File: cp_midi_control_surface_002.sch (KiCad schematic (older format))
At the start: 37 parts, among them P1 Power, P2 Analogue, P3 Digital, P4 Communication, P5 PWM, P6 PWM

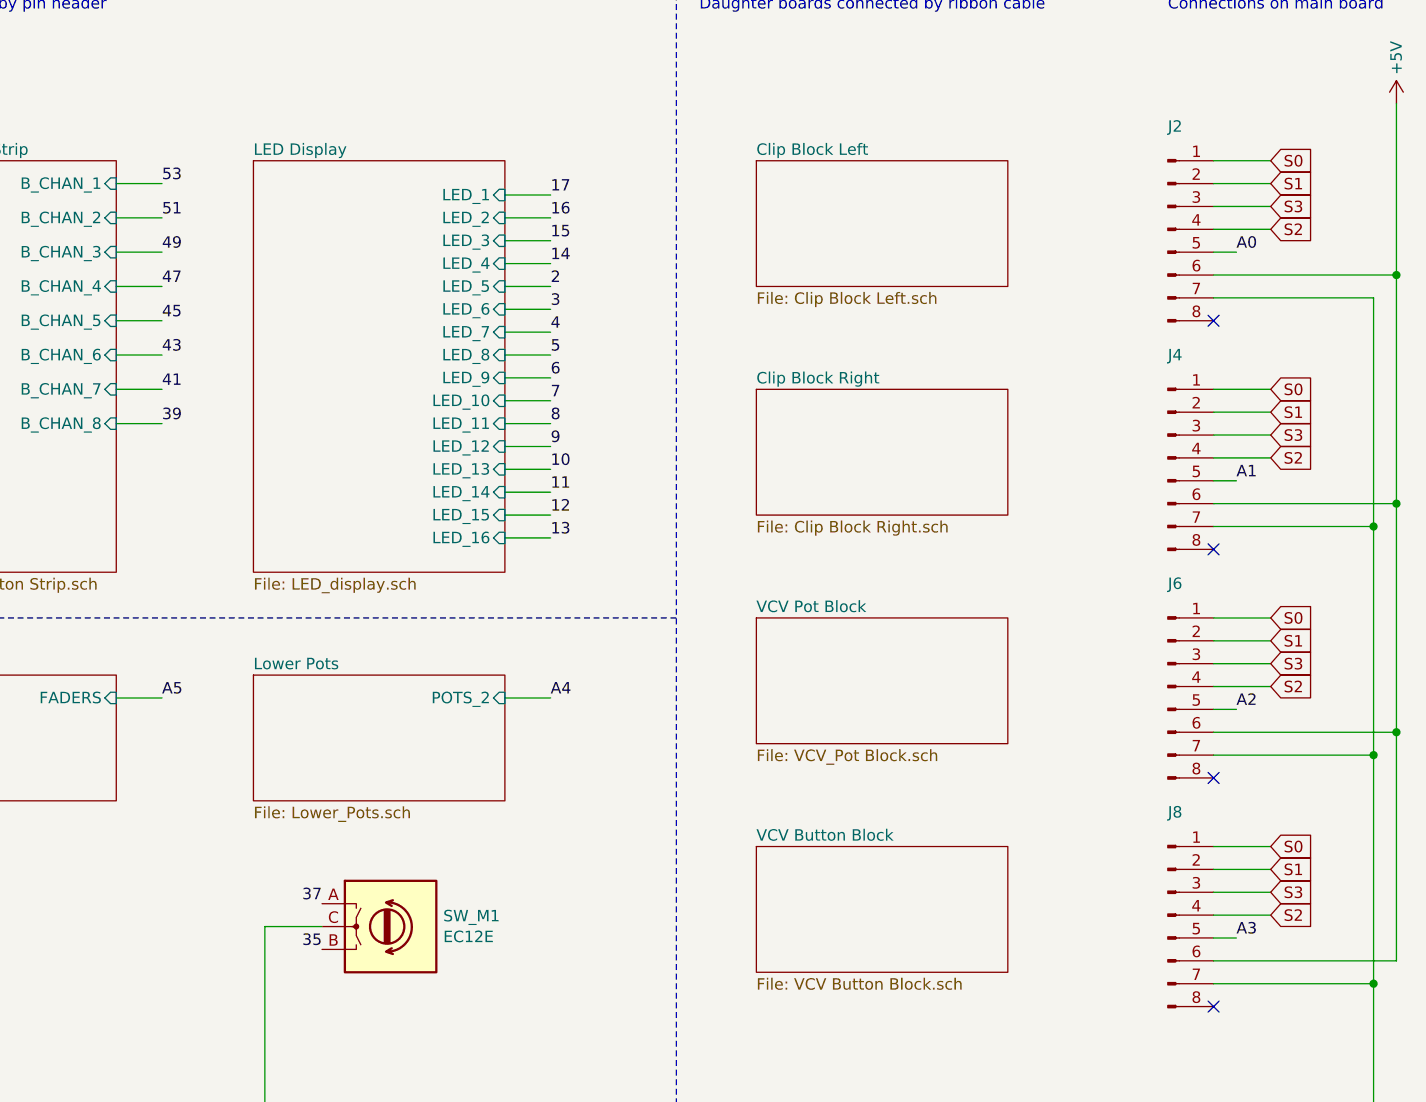
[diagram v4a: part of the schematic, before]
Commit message: Further traces added and reassigned duaghter board connection
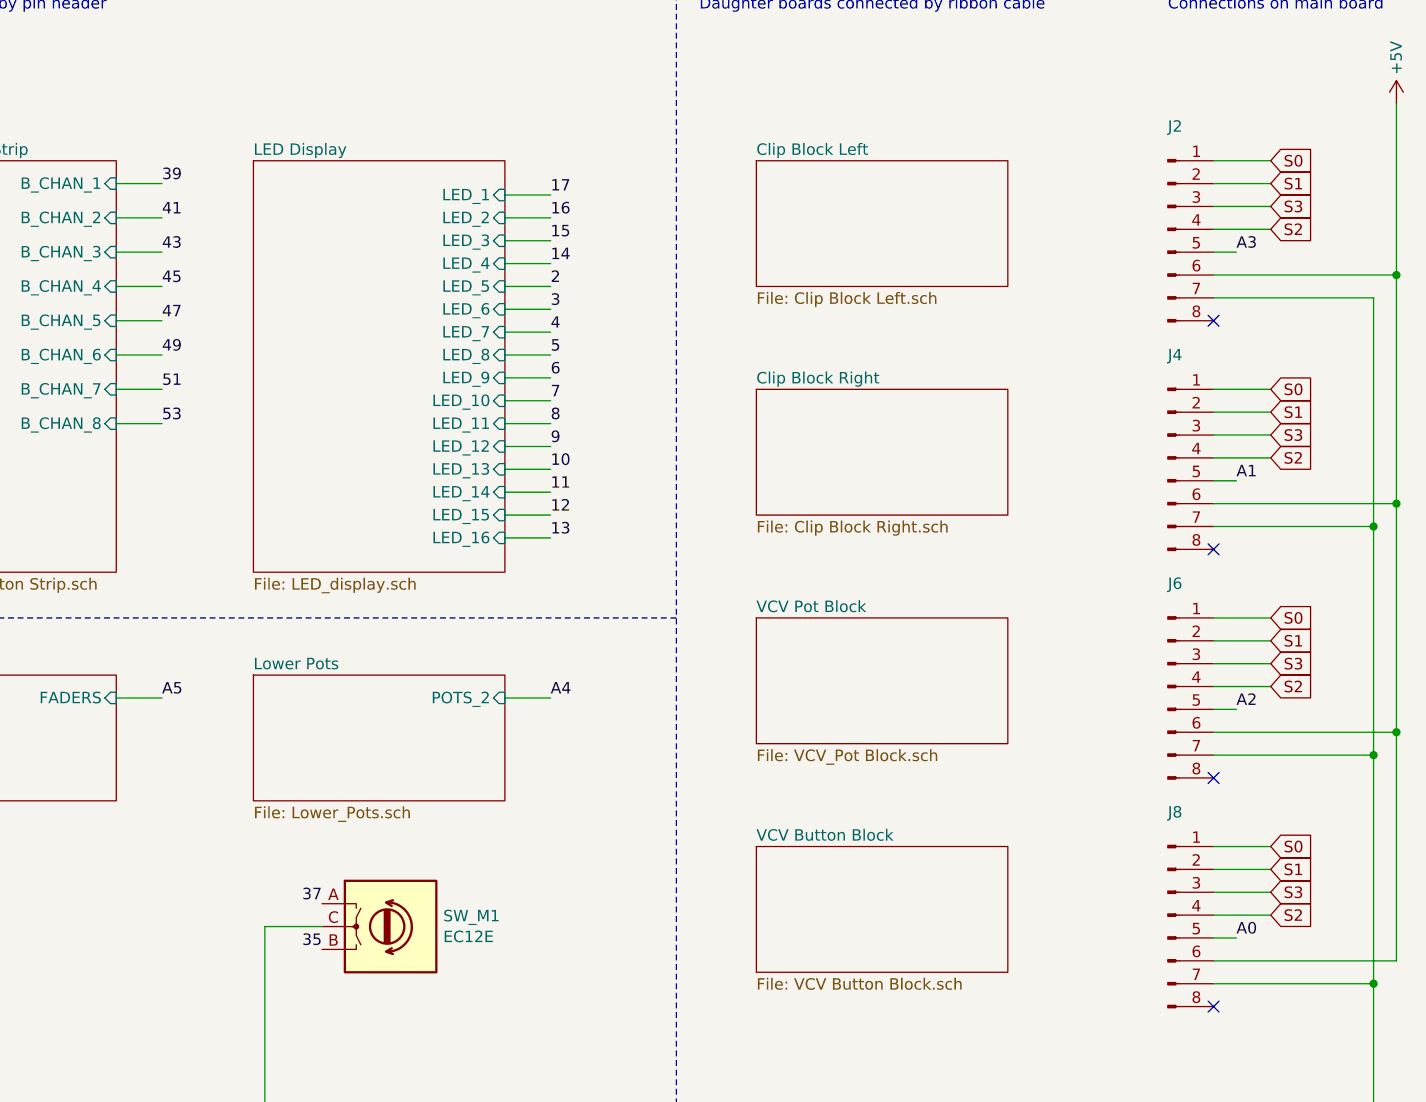
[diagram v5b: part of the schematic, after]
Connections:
- net A0: now also J8.5 (Pin_5); no longer J2.5 (Pin_5)
- net A3: now also J2.5 (Pin_5); no longer J8.5 (Pin_5)
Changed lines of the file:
@@
 Wire Wire Line
 	2250 2400 2050 2400
+Text Label 2250 2400 0    50   ~ 0
+53
+Text Label 2250 2250 0    50   ~ 0
+51
+Text Label 2250 1950 0    50   ~ 0
+47
+Text Label 2250 2100 0    50   ~ 0
+49
+Text Label 2250 1800 0    50   ~ 0
+45
+Text Label 2250 1650 0    50   ~ 0
+43
+Text Label 2250 1500 0    50   ~ 0
+41
 Text Label 2250 1350 0    50   ~ 0
-53
-Text Label 2250 1500 0    50   ~ 0
-51
-Text Label 2250 1800 0    50   ~ 0
-47
-Text Label 2250 1650 0    50   ~ 0
-49
-Text Label 2250 1950 0    50   ~ 0
-45
-Text Label 2250 2100 0    50   ~ 0
-43
-Text Label 2250 2250 0    50   ~ 0
-41
-Text Label 2250 2400 0    50   ~ 0
 39
 NoConn ~ 10450 3750
@@
 Wire Wire Line
 	8650 5050 8650 5750
-Text Label 6950 1650 0    50   ~ 0
+Text Label 6950 4650 0    50   ~ 0
 A0
 $Comp
@@
 	7550 2850 6850 2850
 NoConn ~ 6850 2950
-Text Label 6950 4650 0    50   ~ 0
+Text Label 6950 1650 0    50   ~ 0
 A3
 $Comp

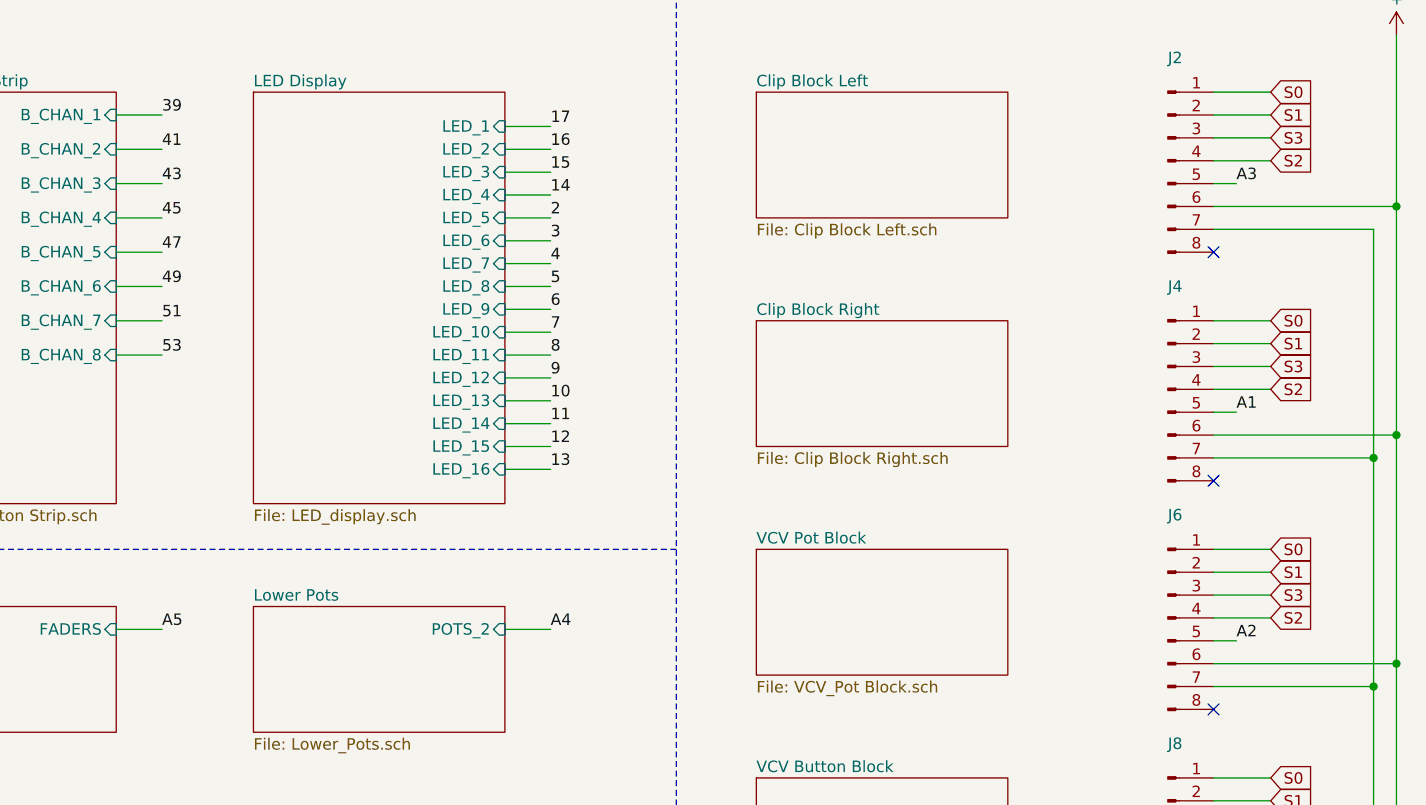
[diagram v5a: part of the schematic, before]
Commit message: Connections complete
All traces mapped and DRC passed apart from interboard errors - should look into fixing those.
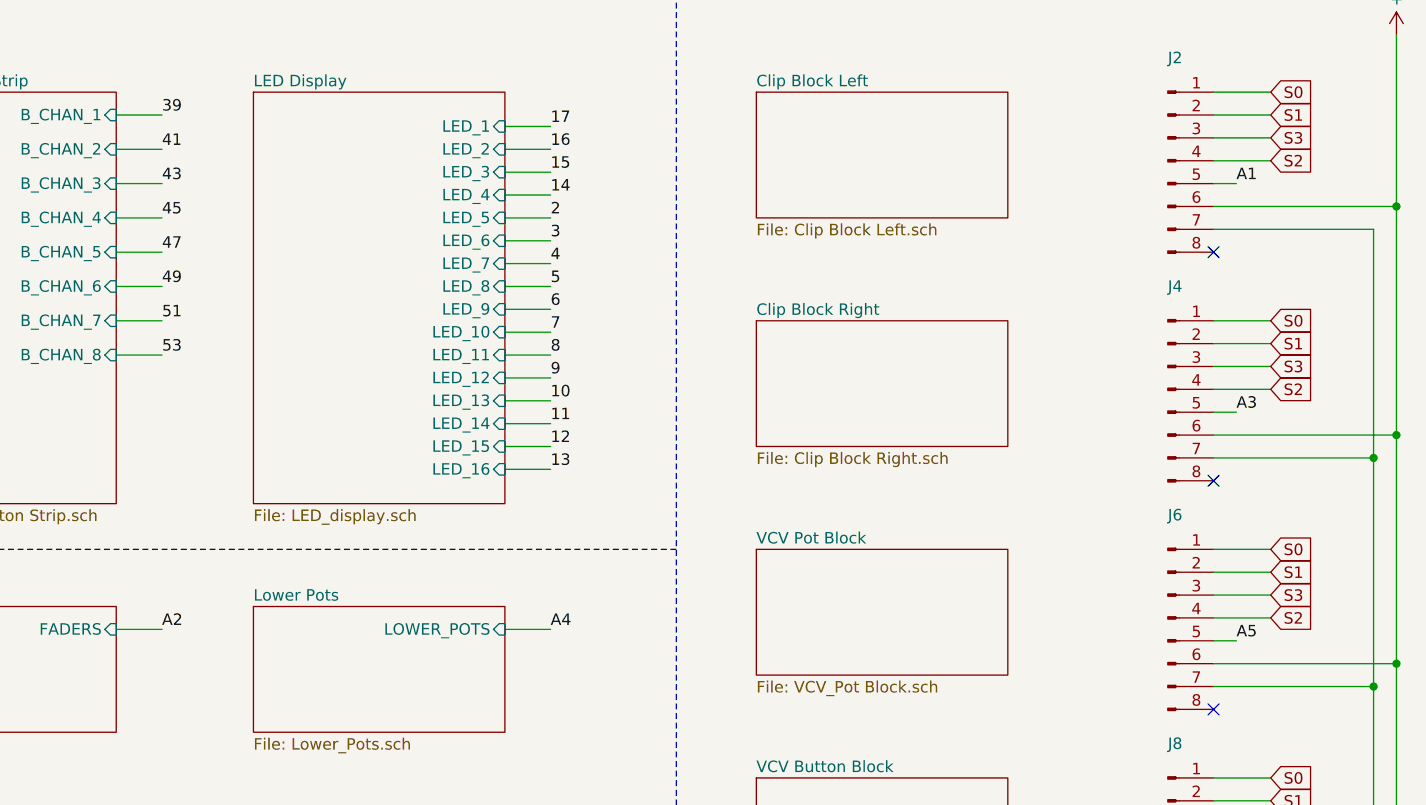
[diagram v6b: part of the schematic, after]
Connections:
- net A1: now also J2.5 (Pin_5); no longer J4.5 (Pin_5)
- net A2: no longer J6.5 (Pin_5)
- net A3: now also J4.5 (Pin_5); no longer J2.5 (Pin_5)
- net A5: now also J6.5 (Pin_5)
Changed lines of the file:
@@
 F0 "Lower Pots" 50
 F1 "Lower_Pots.sch" 0
-F2 "POTS_2" I R 3750 3600 50
+F2 "LOWER_POTS" I R 3750 3600 50
 $EndSheet
 $Sheet
@@
 NoConn ~ 6850 1950
 Text Label 6950 3650 0    50   ~ 0
-A2
+A5
 $Comp
 L Connector:Conn_01x08_Male J6
@@
 NoConn ~ 6850 3950
 Text Label 6950 2650 0    50   ~ 0
-A1
+A3
 $Comp
 L Connector:Conn_01x08_Male J4
@@
 NoConn ~ 6850 2950
 Text Label 6950 1650 0    50   ~ 0
-A3
+A1
 $Comp
 L Connector:Conn_01x08_Male J8
@@
 	10500 4850 10500 5050
 Text Label 2250 3600 0    50   ~ 0
-A5
+A2
 Wire Wire Line
 	2050 3600 2250 3600

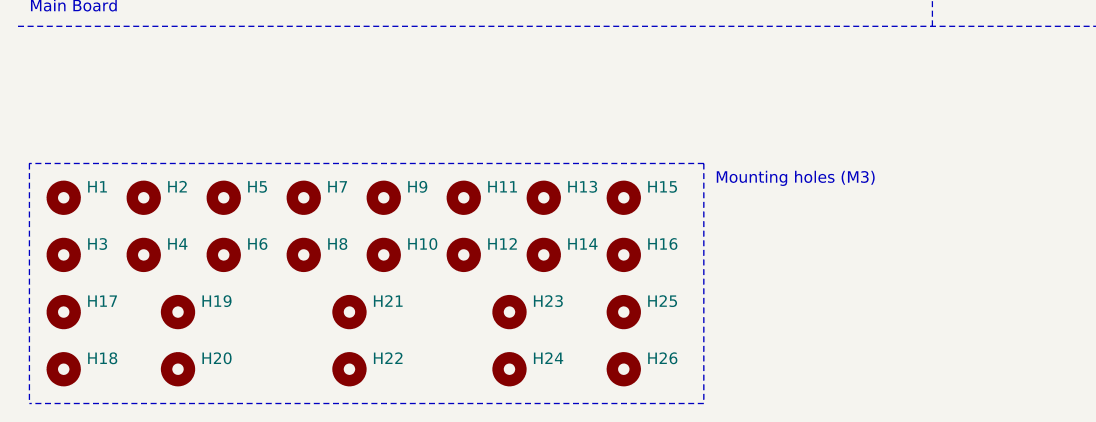
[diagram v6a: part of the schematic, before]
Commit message: Resize boards and update connector
Resized the boards to fit the new modular height and started changing the interboard connectors
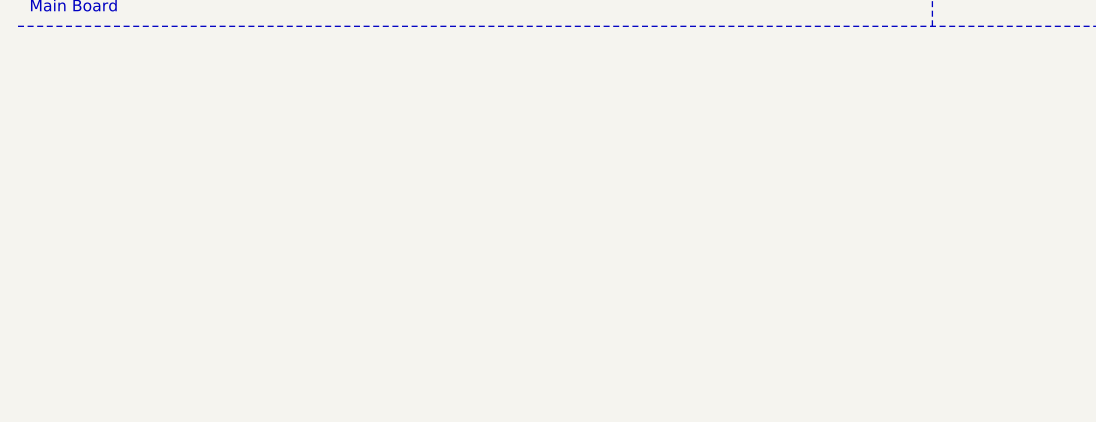
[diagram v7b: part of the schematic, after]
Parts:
- removed H1, H10, H11, H12, H13, H14, H15, H16, H17, H18, H19, H2, H20, H21, H22, H23, H24, H25, H26, H3, H4, H5, H6, H7, H8, H9: ~, cunabulapress-footprints:Mounting_Hole_M3_with_Target, symbol Mechanical:MountingHole
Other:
- note removed: "Mounting holes (M3)"

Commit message: Further cleanup and placement
Removed all the connectors to the rails as they're irrelevant to the top boards.

Added all the support headers.

Need to work out the correct routing for the headers but the placement is correct.
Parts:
- added JX13, JX14, JX15, JX16, JX17, JX18, JX19, JX20, JX21, JX22, JX23, JX24: Conn_02x03_Odd_Even, Connector_PinHeader_2.54mm:PinHeader_2x03_P2.54mm_Vertical, symbol Connector_Generic:Conn_02x03_Odd_Even
- JA2: renamed from J2; footprint cunabulapress-footprints:Connector_TE_Connectivity_Micro-MaTch_8_Position_Female -> Connector_PinHeader_2.54mm:PinHeader_2x03_P2.54mm_Vertical; symbol Connector:Conn_01x08_Male -> Connector:Conn_01x06_Male
- JA4: renamed from J4; footprint cunabulapress-footprints:Connector_TE_Connectivity_Micro-MaTch_8_Position_Female -> Connector_PinHeader_2.54mm:PinHeader_2x03_P2.54mm_Vertical; symbol Connector:Conn_01x08_Male -> Connector:Conn_01x06_Male
- JA6: renamed from J6; footprint cunabulapress-footprints:Connector_TE_Connectivity_Micro-MaTch_8_Position_Female -> Connector_PinHeader_2.54mm:PinHeader_2x03_P2.54mm_Vertical; symbol Connector:Conn_01x08_Male -> Connector:Conn_01x06_Male
- JA8: renamed from J8; footprint cunabulapress-footprints:Connector_TE_Connectivity_Micro-MaTch_8_Position_Female -> Connector_PinHeader_2.54mm:PinHeader_2x03_P2.54mm_Vertical; symbol Connector:Conn_01x08_Male -> Connector:Conn_01x06_Male
- P3: footprint Connector_PinHeader_2.54mm:PinHeader_1x18_P2.54mm_Vertical -> Connector_PinHeader_2.54mm:PinHeader_2x18_P2.54mm_Vertical; symbol Connector_Generic:Conn_01x18 -> Connector_Generic:Conn_02x18_Odd_Even
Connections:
- net +5V: now also P3.35 (Pin_35), P3.36 (Pin_36); no longer P3.18 (Pin_18)
- net 35: now also P3.22 (Pin_22); no longer P3.11 (Pin_11)
- net 37: now also P3.20 (Pin_20); no longer P3.10 (Pin_10)
- net 39: now also P3.18 (Pin_18); no longer P3.9 (Pin_9)
- net 41: now also P3.16 (Pin_16); no longer P3.8 (Pin_8)
- net 43: now also P3.14 (Pin_14); no longer P3.7 (Pin_7)
- net 45: now also P3.12 (Pin_12); no longer P3.6 (Pin_6)
- net 47: now also P3.10 (Pin_10); no longer P3.5 (Pin_5)
- net 49: now also P3.8 (Pin_8); no longer P3.4 (Pin_4)
- net 51: now also P3.6 (Pin_6); no longer P3.3 (Pin_3)
- net 53: now also P3.4 (Pin_4); no longer P3.2 (Pin_2)
- net GND: now also P3.2 (Pin_2), JX13.1 (Pin_1), JX13.2 (Pin_2), JX13.3 (Pin_3), JX13.4 (Pin_4), JX13.5 (Pin_5), JX13.6 (Pin_6), JX14.1 (Pin_1), JX14.2 (Pin_2), JX14.3 (Pin_3), JX14.4 (Pin_4), JX14.5 (Pin_5), JX14.6 (Pin_6), JX15.1 (Pin_1), JX15.2 (Pin_2), JX15.3 (Pin_3), JX15.4 (Pin_4), JX15.5 (Pin_5), JX15.6 (Pin_6), JX16.1 (Pin_1), JX16.2 (Pin_2), JX16.3 (Pin_3), JX16.4 (Pin_4), JX16.5 (Pin_5), JX16.6 (Pin_6); no longer JA2.7 (Pin_7), JA4.7 (Pin_7), JA6.7 (Pin_7), JA8.7 (Pin_7)
- net S0: now also P3.34 (Pin_34); no longer P3.17 (Pin_17)
- net S1: now also P3.32 (Pin_32); no longer P3.16 (Pin_16)
- net S2: now also P3.28 (Pin_28); no longer P3.14 (Pin_14)
- net S3: now also P3.30 (Pin_30); no longer P3.15 (Pin_15)
- no-connect marks 19 -> 79
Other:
- note added: "Daughter boards"
- note removed: "Daughter boards connected by ribbon cable"
